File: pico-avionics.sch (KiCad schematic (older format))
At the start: 33 parts, among them J1 Parachute, J2 UC Debug PWR, M1 Servo X, M2 Servo Y, Q1 IRF540N, SW1 SW_SPDT, U1 LM1086-3.3, U2 L7805CV, U3 L7805CV, U4 Pico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

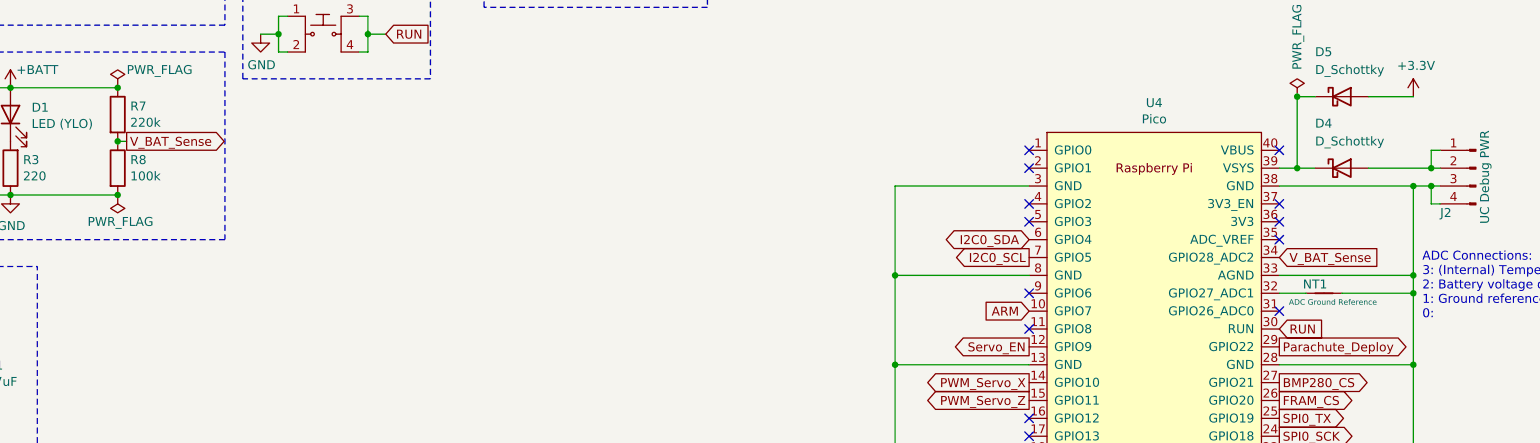
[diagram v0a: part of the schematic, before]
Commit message: Update nets to work with pinout
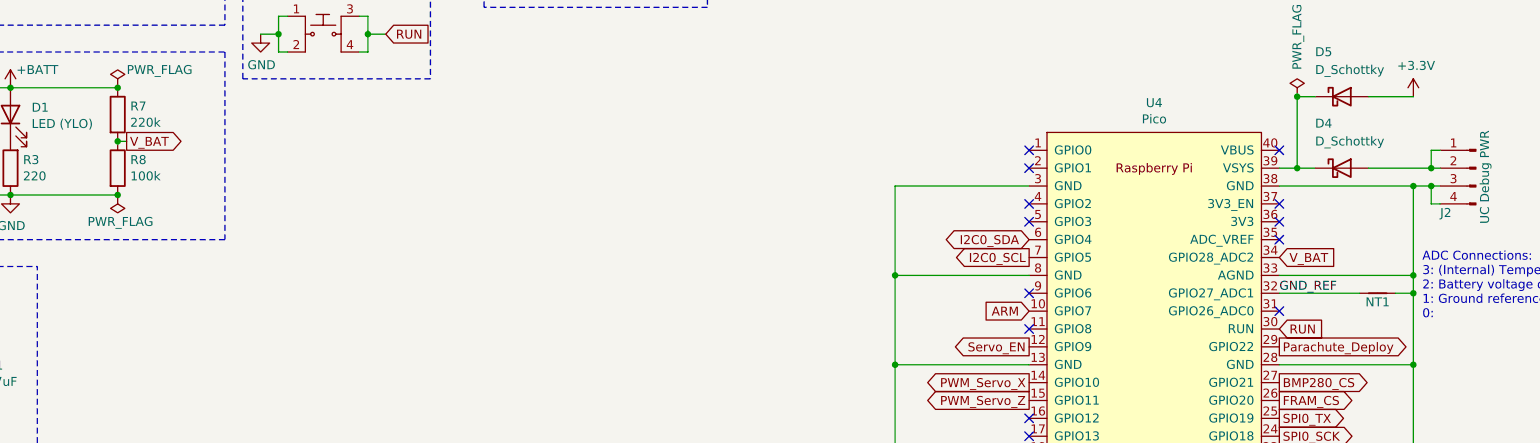
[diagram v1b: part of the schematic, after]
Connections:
- net GND_REF: now reaches NT1.2, U4.32 (GPIO27_ADC1)
- net V_BAT_Sense renamed V_BAT
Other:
- moved on the sheet: NT1
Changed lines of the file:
@@
 Connection ~ 1900 4550
 Text GLabel 2550 4850 2    50   Output ~ 0
-V_BAT_Sense
+V_BAT
 Wire Wire Line
 	2500 4850 2550 4850
@@
 PWM_Servo_Z
 Text GLabel 9000 5500 2    50   Input ~ 0
-V_BAT_Sense
-Wire Wire Line
-	9000 5700 9150 5700
+V_BAT
 $Comp
 L power:+3.3V #PWR023
@@
 Text Notes 9800 5850 0    50   ~ 0
 ADC Connections:\n3: (Internal) Temperature Sensor\n2: Battery voltage divider\n1: Ground reference\n0:
-$Comp
-L Device:Net-Tie_2 NT1
-U 1 1 608A8144
-P 9250 5700
-F 0 "NT1" H 9300 5650 50  0000 C CNN
-F 1 "ADC Ground Reference" H 9200 5750 31  0000 C CNN
-F 2 "NetTie:NetTie-2_SMD_Pad0.5mm" H 9250 5700 50  0001 C CNN
-F 3 "~" H 9250 5700 50  0001 C CNN
-	1    9250 5700
-	-1   0    0    1
-$EndComp
 Wire Wire Line
 	9750 7100 9750 6600
@@
 	9750 5700 9750 6100
 Connection ~ 9750 5700
-Wire Wire Line
-	9350 5700 9750 5700
 Wire Wire Line
 	9750 5100 9750 5600
@@
 	-1   0    0    -1
 $EndComp
+Text Label 9000 5700 0    50   ~ 0
+GND_REF
+Wire Wire Line
+	9650 5700 9750 5700
+$Comp
+L Device:Net-Tie_2 NT1
+U 1 1 608A8144
+P 9550 5700
+F 0 "NT1" H 9550 5750 50  0000 C CNN
+F 1 "ADC Ground Reference" H 9500 5750 31  0001 C CNN
+F 2 "NetTie:NetTie-2_SMD_Pad0.5mm" H 9550 5700 50  0001 C CNN
+F 3 "~" H 9550 5700 50  0001 C CNN
+	1    9550 5700
+	-1   0    0    1
+$EndComp
+Wire Wire Line
+	9000 5700 9450 5700
 Wire Bus Line
 	13800 1000 13800 4650
